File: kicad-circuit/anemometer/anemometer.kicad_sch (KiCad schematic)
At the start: 51 parts, among them J5VIN1 Conn_01x03, J5VIN2 Conn_01x03, Q1 TIP41, Q2 2N3906, U1 LM358, U2 LM324

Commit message: Corrected the thermistor temperature circuit.
There was a mistake. I corrected it ion the board that I built and now it is corrected in the Kicad circuit.
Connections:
- net GND: now also JTemp1.2 (Pin_2)
- net at RT1.2: now also JTemp1.1 (Pin_1), U1.3 (+); no longer JTemp1.2 (Pin_2)
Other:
- moved on the sheet: JTemp1
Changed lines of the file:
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@@
   (junction (at 31.75 138.43) (diameter 0) (color 0 0 0 0)
+  )
+  (junction (at 35.56 163.83) (diameter 0) (color 0 0 0 0)
   )
   (junction (at 109.22 124.46) (diameter 0) (color 0 0 0 0)
@@
     (stroke (width 0) (type default) (color 0 0 0 0))
   )
+  (wire (pts (xy 55.88 160.02) (xy 55.88 170.18))
+    (stroke (width 0) (type default) (color 0 0 0 0))
+  )
   (wire (pts (xy 78.74 135.89) (xy 78.74 147.32))
     (stroke (width 0) (type default) (color 0 0 0 0))
@@
     (stroke (width 0) (type default) (color 0 0 0 0))
   )
-  (wire (pts (xy 55.88 166.37) (xy 55.88 170.18))
-    (stroke (width 0) (type default) (color 0 0 0 0))
-  )
   (wire (pts (xy 102.87 181.61) (xy 118.11 181.61))
     (stroke (width 0) (type default) (color 0 0 0 0))
@@
     (stroke (width 0) (type default) (color 0 0 0 0))
   )
+  (wire (pts (xy 38.1 166.37) (xy 38.1 167.64))
+    (stroke (width 0) (type default) (color 0 0 0 0))
+  )
   (wire (pts (xy 43.18 143.51) (xy 43.18 135.89))
     (stroke (width 0) (type default) (color 0 0 0 0))
@@
     (stroke (width 0) (type default) (color 0 0 0 0))
   )
-  (wire (pts (xy 38.1 166.37) (xy 55.88 166.37))
-    (stroke (width 0) (type default) (color 0 0 0 0))
-  )
   (wire (pts (xy 104.14 146.05) (xy 104.14 152.4))
     (stroke (width 0) (type default) (color 0 0 0 0))
@@
     (stroke (width 0) (type default) (color 0 0 0 0))
   )
+  (wire (pts (xy 35.56 163.83) (xy 35.56 160.02))
+    (stroke (width 0) (type default) (color 0 0 0 0))
+  )
   (wire (pts (xy 91.44 181.61) (xy 91.44 175.26))
     (stroke (width 0) (type default) (color 0 0 0 0))
@@
     (stroke (width 0) (type default) (color 0 0 0 0))
   )
+  (wire (pts (xy 35.56 163.83) (xy 35.56 167.64))
+    (stroke (width 0) (type default) (color 0 0 0 0))
+  )
   (wire (pts (xy 118.11 142.24) (xy 118.11 140.97))
     (stroke (width 0) (type default) (color 0 0 0 0))
@@
     (stroke (width 0) (type default) (color 0 0 0 0))
   )
-  (wire (pts (xy 35.56 163.83) (xy 35.56 166.37))
-    (stroke (width 0) (type default) (color 0 0 0 0))
-  )
   (wire (pts (xy 157.48 161.29) (xy 157.48 177.8))
     (stroke (width 0) (type default) (color 0 0 0 0))
@@
   )
   (wire (pts (xy 36.83 71.12) (xy 39.37 71.12))
+    (stroke (width 0) (type default) (color 0 0 0 0))
+  )
+  (wire (pts (xy 35.56 160.02) (xy 55.88 160.02))
     (stroke (width 0) (type default) (color 0 0 0 0))
   )
@@
     (pin "3")
   )
+  (symbol (lib_id "power:GND") (at 38.1 166.37 180) (unit 1)
+    (in_bom yes) (on_board yes)
+    (property "Reference" "#PWR0132" (id 0) (at 38.1 160.02 0)
+      (effects (font (size 1.27 1.27)) hide)
+    )
+    (property "Value" "GND" (id 1) (at 37.973 161.9758 0))
+    (property "Footprint" "" (id 2) (at 38.1 166.37 0)
+      (effects (font (size 1.27 1.27)) hide)
+    )
+    (property "Datasheet" "" (id 3) (at 38.1 166.37 0)
+      (effects (font (size 1.27 1.27)) hide)
+    )
+    (pin "1")
+  )
   (symbol (lib_id "Amplifier_Operational:LM324") (at 135.89 139.7 0) (unit 1)
     (in_bom yes) (on_board yes) (fields_autoplaced)
@@
     (pin "8")
   )
-  (symbol (lib_id "Connector_Generic:Conn_01x02") (at 38.1 171.45 270) (unit 1)
-    (in_bom yes) (on_board yes) (fields_autoplaced)
-    (property "Reference" "JTemp1" (id 0) (at 40.64 170.1799 90)
-      (effects (font (size 1.27 1.27)) (justify left))
-    )
-    (property "Value" "Conn_01x02" (id 1) (at 40.64 172.7199 90)
-      (effects (font (size 1.27 1.27)) (justify left))
-    )
-    (property "Footprint" "TerminalBlock:TerminalBlock_bornier-2_P5.08mm" (id 2) (at 38.1 171.45 0)
-      (effects (font (size 1.27 1.27)) hide)
-    )
-    (property "Datasheet" "~" (id 3) (at 38.1 171.45 0)
+  (symbol (lib_id "Connector_Generic:Conn_01x02") (at 35.56 172.72 90) (mirror x) (unit 1)
+    (in_bom yes) (on_board yes) (fields_autoplaced)
+    (property "Reference" "JTemp1" (id 0) (at 40.64 171.4499 90)
+      (effects (font (size 1.27 1.27)) (justify right))
+    )
+    (property "Value" "Conn_01x02" (id 1) (at 40.64 173.9899 90)
+      (effects (font (size 1.27 1.27)) (justify right))
+    )
+    (property "Footprint" "TerminalBlock:TerminalBlock_bornier-2_P5.08mm" (id 2) (at 35.56 172.72 0)
+      (effects (font (size 1.27 1.27)) hide)
+    )
+    (property "Datasheet" "~" (id 3) (at 35.56 172.72 0)
       (effects (font (size 1.27 1.27)) hide)
     )
@@
       (reference "#PWR0131") (unit 1) (value "GND") (footprint "")
     )
+    (path "/b643752e-d915-464b-9315-70477dc6ddff"
+      (reference "#PWR0132") (unit 1) (value "GND") (footprint "")
+    )
     (path "/71cd9d38-225b-4bd1-af58-80b5992341e4"

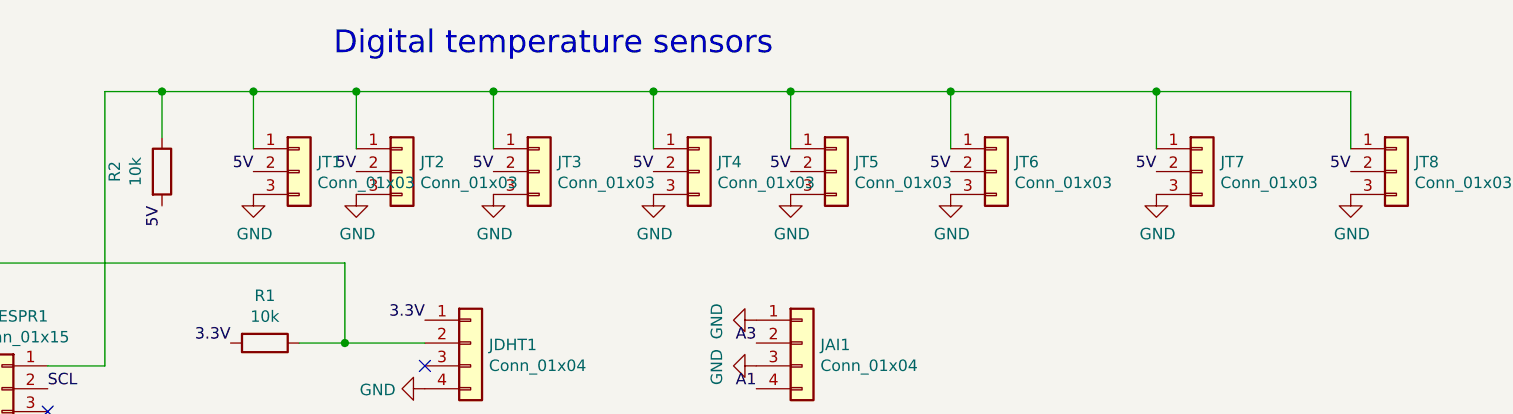
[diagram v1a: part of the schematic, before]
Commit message: Switched pins of DS18B20 temp. sensor
Now the tracks are positioned in the same orientation as the pins in the TO-92 packaging. Not important but now I can solder one sensor directly on the board.
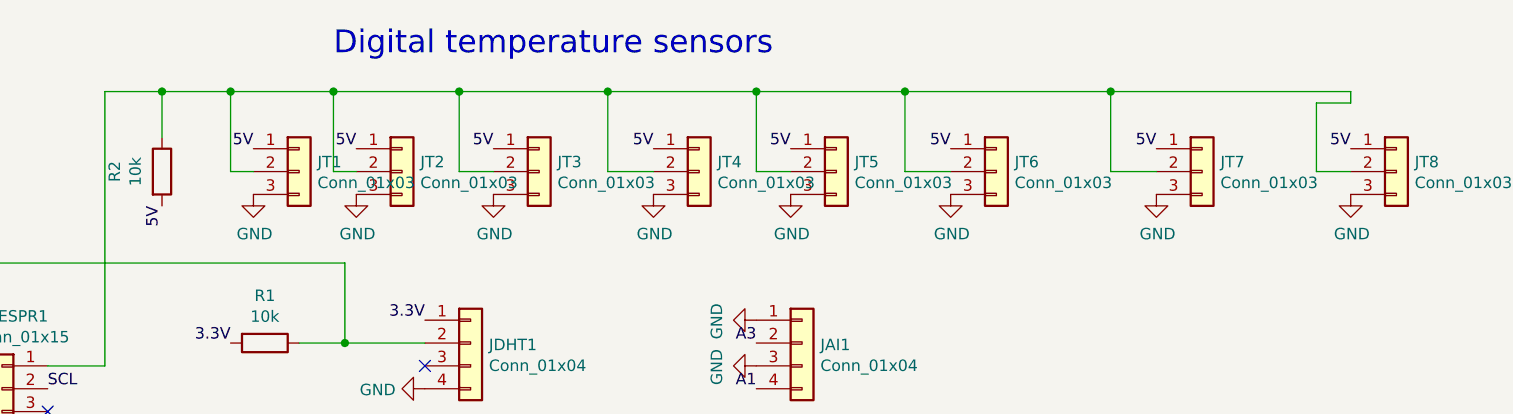
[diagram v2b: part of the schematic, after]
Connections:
- net 5V: now also JT1.1 (Pin_1), JT2.1 (Pin_1), JT3.1 (Pin_1), JT4.1 (Pin_1), JT5.1 (Pin_1), JT6.1 (Pin_1), JT7.1 (Pin_1), JT8.1 (Pin_1); no longer JT1.2 (Pin_2), JT2.2 (Pin_2), JT3.2 (Pin_2), JT4.2 (Pin_2), JT5.2 (Pin_2), JT6.2 (Pin_2), JT7.2 (Pin_2), JT8.2 (Pin_2)
- new net: JESPR1.1 (Pin_1), JT1.2 (Pin_2), JT2.2 (Pin_2), JT3.2 (Pin_2), JT4.2 (Pin_2), JT5.2 (Pin_2), JT6.2 (Pin_2), JT7.2 (Pin_2), JT8.2 (Pin_2), R2.1

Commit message: Moved some components so that the TIP41 transistor can lay on its back
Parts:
- Q1: footprint Package_TO_SOT_THT:TO-220-3_Vertical -> Package_TO_SOT_THT:TO-220-3_Horizontal_TabUp
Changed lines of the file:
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@@
       (effects (font (size 1.27 1.27)) (justify left))
     )
-    (property "Footprint" "Package_TO_SOT_THT:TO-220-3_Vertical" (id 2) (at 105.41 120.015 0)
+    (property "Footprint" "Package_TO_SOT_THT:TO-220-3_Horizontal_TabUp" (id 2) (at 105.41 120.015 0)
       (effects (font (size 1.27 1.27) italic) (justify left) hide)
     )
@@
     )
     (path "/1f6a499a-1e9f-4ade-8afd-a1205c7b8f1e"
-      (reference "Q1") (unit 1) (value "TIP41") (footprint "Package_TO_SOT_THT:TO-220-3_Vertical")
+      (reference "Q1") (unit 1) (value "TIP41") (footprint "Package_TO_SOT_THT:TO-220-3_Horizontal_TabUp")
     )
     (path "/065ced61-e115-41c1-966a-4568244b436a"
